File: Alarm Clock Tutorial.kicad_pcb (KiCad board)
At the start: 2 copper layers, 49 x 46 mm, 21 parts, among them K1 DIP-SWITCH-TACTILE-SPST-NO_TS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, K2 DIP-SWITCH-TACTILE-SPST-NO_TS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, K3 DIP-SWITCH-TACTILE-SPST-NO_TS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, U1 MCU-ATMEGA32U4-AU_TQFP44_, U2 LED-4-BETY-7-SEG_2X7P-30X14MM_

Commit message: This version was ordered from Seeed Studio
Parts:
- added C3: 12-22pF, SeeedOPL-Capacitor-2016:CERAMIC-2.54, F.Cu at (155.5, 92.2)
- added C4: 12-22pF, SeeedOPL-Capacitor-2016:CERAMIC-2.54, F.Cu at (155.5, 85.4)
- added Y1: 8-16 MHZ, SeeedOPL-Crystal Oscillator-2016:HC49US, F.Cu at (161.2, 88.5)
- moved K2 6.62 mm to (159.2, 79.5)
- moved K3 6.62 mm to (159.2, 72.0)
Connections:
- K1 pad 1: (no net) -> Net-(K1-Pad1)
- K1 pad 3: (no net) -> Net-(K1-Pad3)
- K2 pad 1: (no net) -> Net-(K2-Pad1)
- K2 pad 2: (no net) -> Net-(K2-Pad2)
- K3 pad 1: (no net) -> Net-(K3-Pad1)
- K3 pad 3: (no net) -> Net-(K3-Pad3)
- U1 pad 10: (no net) -> Net-(U1-Pad10)
- U1 pad 11: (no net) -> Net-(U1-Pad11)
- U1 pad 12: (no net) -> Net-(U1-Pad12)
- U1 pad 16: (no net) -> Net-(C4-Pad2)
- U1 pad 17: (no net) -> Net-(C3-Pad2)
- U1 pad 18: (no net) -> Net-(U1-Pad18)
- U1 pad 19: (no net) -> Net-(U1-Pad19)
- U1 pad 20: (no net) -> Net-(U1-Pad20)
- U1 pad 21: (no net) -> Net-(U1-Pad21)
- U1 pad 22: (no net) -> Net-(U1-Pad22)
- U1 pad 33: (no net) -> Net-(U1-Pad33)
- U1 pad 42: (no net) -> Net-(U1-Pad42)
- U1 pad 8: (no net) -> Net-(U1-Pad8)
- U1 pad 9: (no net) -> Net-(U1-Pad9)
- USB1 pad 4: (no net) -> Net-(USB1-Pad4)
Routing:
- net Net-(C3-Pad2): track 0.00 -> 28.2 mm, vias 0 -> 1
- net Net-(C4-Pad2): track 0.00 -> 27.9 mm, vias 0 -> 1
- net /BTN2: track 6.71 -> 10.8 mm
- net GND: track 150.9 -> 154.9 mm
- net /BTN1: track 9.49 -> 6.76 mm

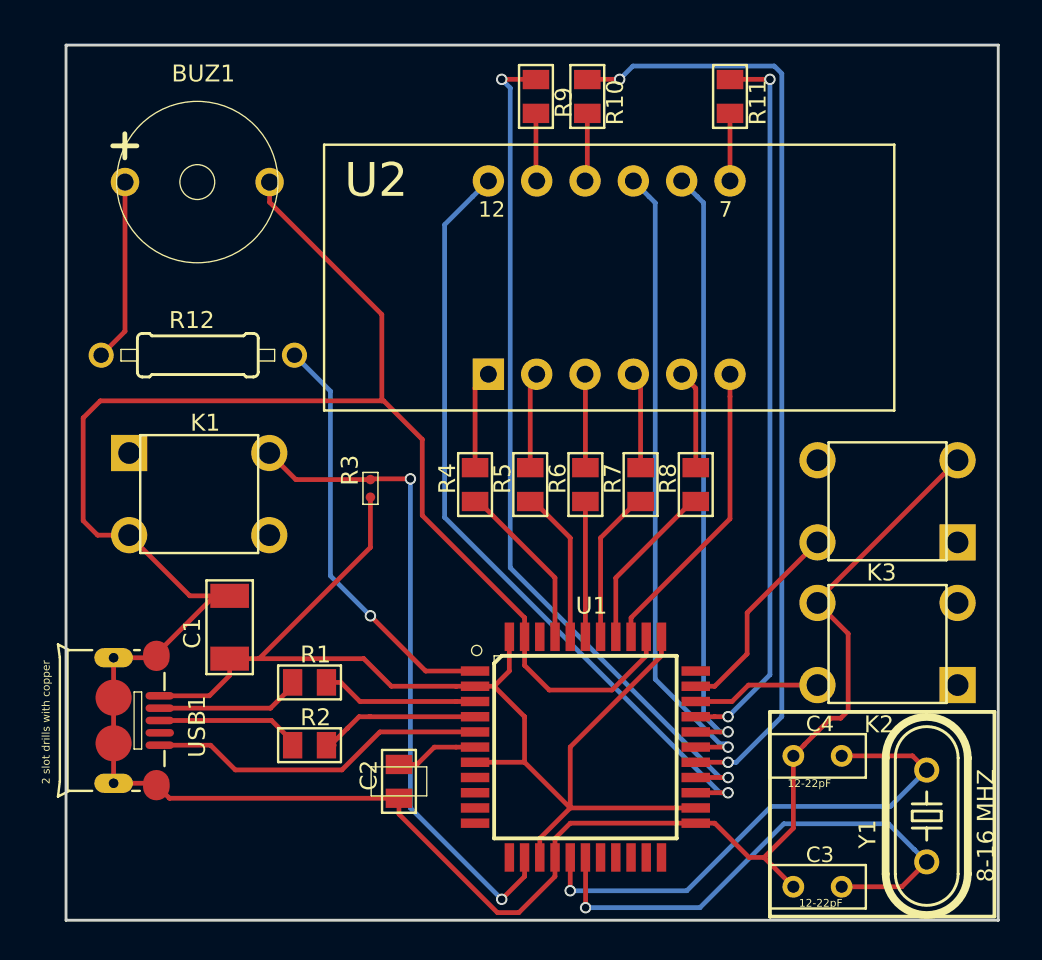
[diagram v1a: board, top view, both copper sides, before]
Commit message: Updated component values on board
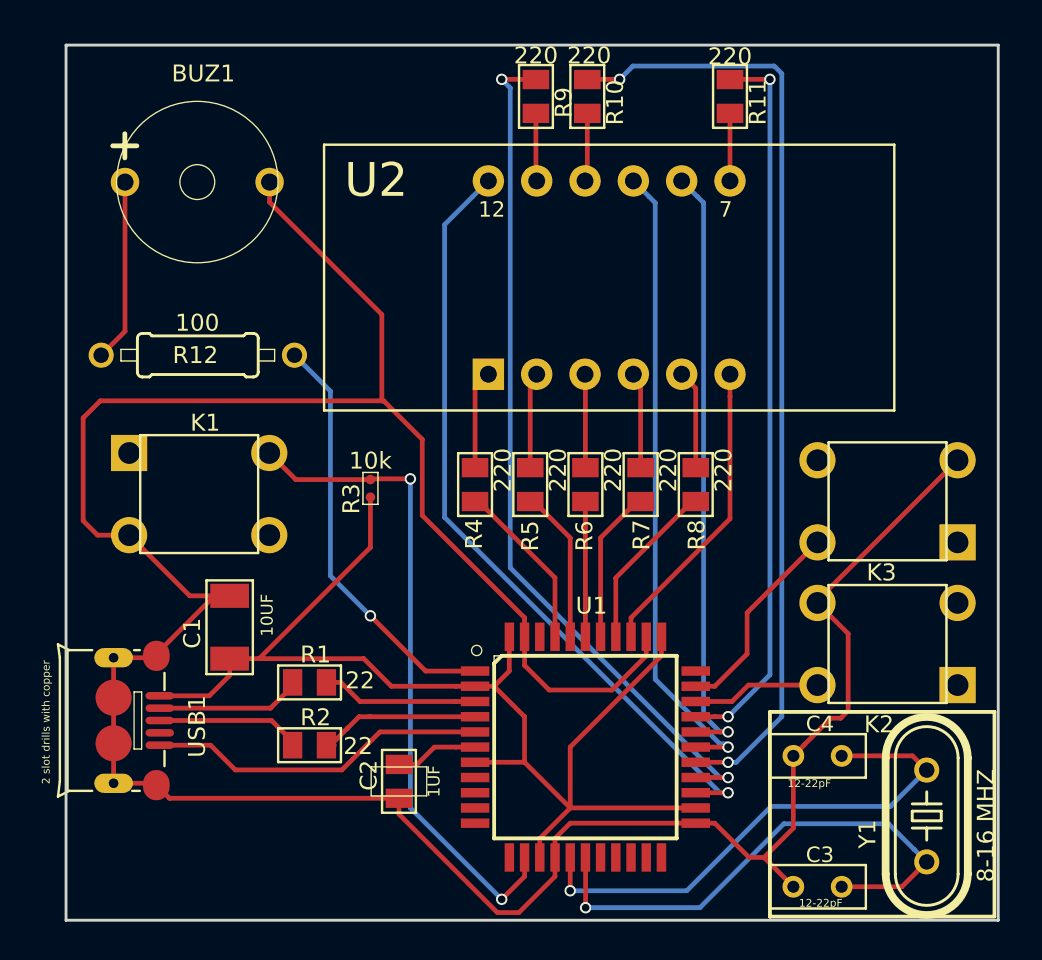
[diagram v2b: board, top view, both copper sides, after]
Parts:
- C1: value CERAMIC-10UF-25V-10%-X5R_1206_ -> 10UF
- C2: value CERAMIC-1UF-25V-10%-X7R_0805_ -> 1UF
- R1, R2: value SMD-RES-22R-5%-1_8W_0805_ -> 22
- R10, R11, R4, R5, R6, R7, R8, R9: value SMD-RES-220R-5%-1_8W_0805_ -> 220
- R12: value DIP-RES-100R-5%-1_4W_PR-D2.3XL6.5MM_ -> 100
- R3: value SMD-RES-10K-1%-1_16W_0402_ -> 10k
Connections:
- K1 pad 1: Net-(K1-Pad1) -> (no net)
- K1 pad 3: Net-(K1-Pad3) -> (no net)
- K2 pad 1: Net-(K2-Pad1) -> (no net)
- K2 pad 2: Net-(K2-Pad2) -> (no net)
- K3 pad 1: Net-(K3-Pad1) -> (no net)
- K3 pad 3: Net-(K3-Pad3) -> (no net)
- U1 pad 10: Net-(U1-Pad10) -> (no net)
- U1 pad 11: Net-(U1-Pad11) -> (no net)
- U1 pad 12: Net-(U1-Pad12) -> (no net)
- U1 pad 18: Net-(U1-Pad18) -> (no net)
- U1 pad 19: Net-(U1-Pad19) -> (no net)
- U1 pad 20: Net-(U1-Pad20) -> (no net)
- U1 pad 21: Net-(U1-Pad21) -> (no net)
- U1 pad 22: Net-(U1-Pad22) -> (no net)
- U1 pad 33: Net-(U1-Pad33) -> (no net)
- U1 pad 42: Net-(U1-Pad42) -> (no net)
- U1 pad 8: Net-(U1-Pad8) -> (no net)
- U1 pad 9: Net-(U1-Pad9) -> (no net)
- USB1 pad 4: Net-(USB1-Pad4) -> (no net)
